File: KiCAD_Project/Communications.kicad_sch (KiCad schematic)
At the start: 19 parts, among them J14 1-0000050, J15 1-0000190, U10 1-0000785, U11 1-0000446

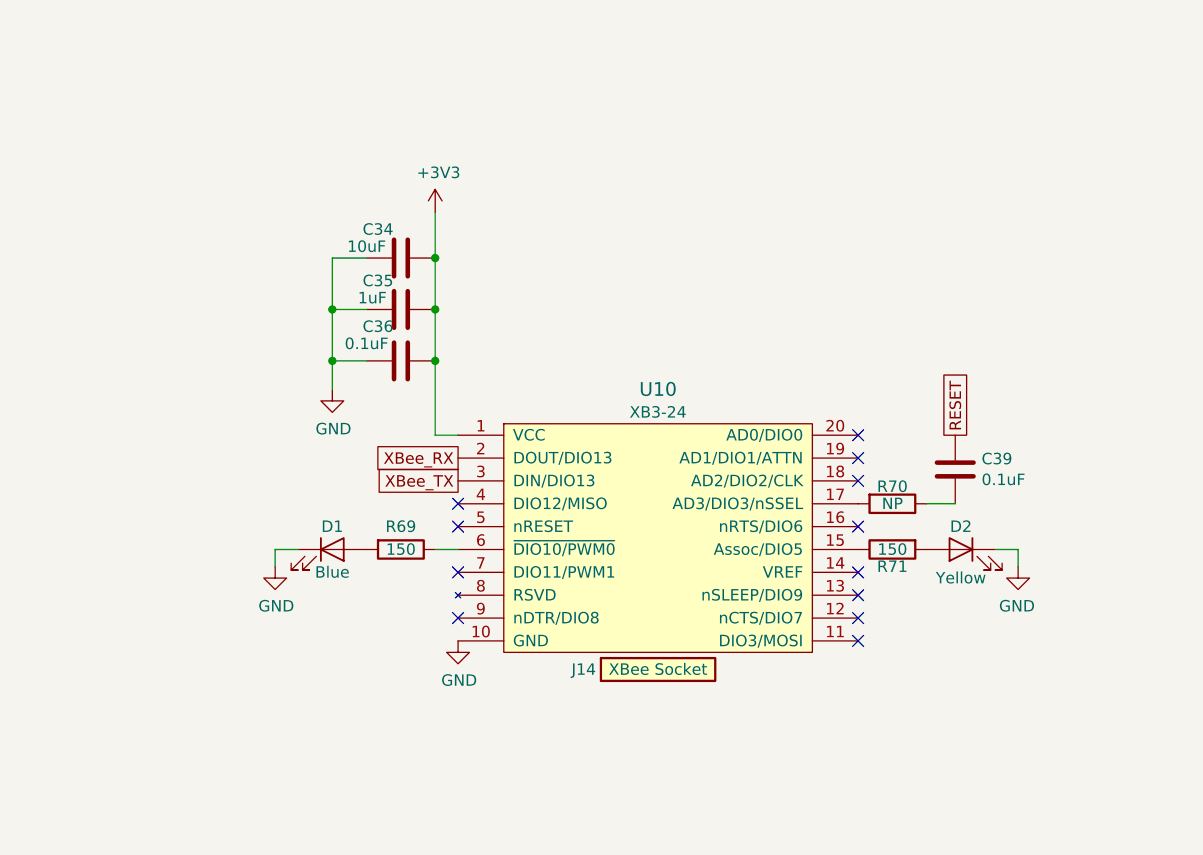
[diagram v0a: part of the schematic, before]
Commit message: Issue #2 (NP on all XBEE parts, J3 changed to SMPL)
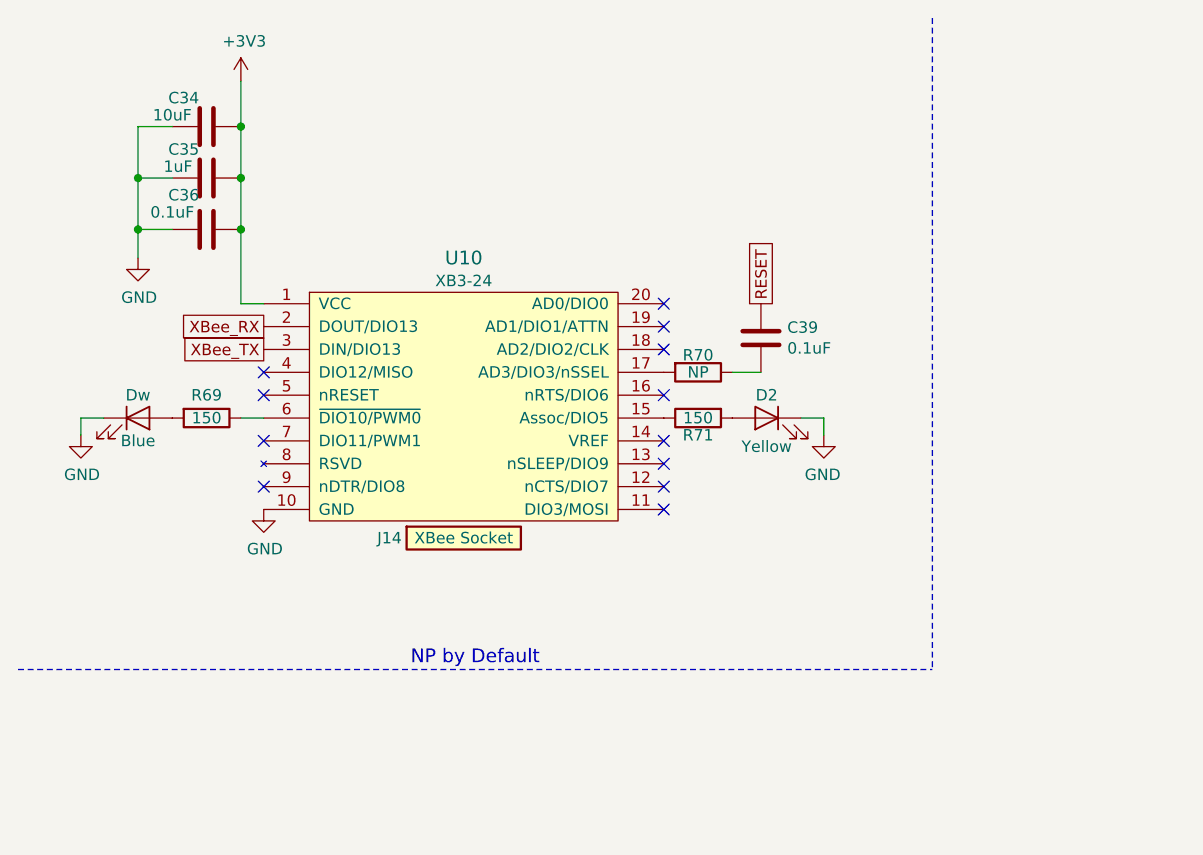
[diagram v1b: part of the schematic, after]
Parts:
- C34, C35, C36, J14, R69: Populated 1 -> 0
- Dw: renamed from D1; Populated 1 -> 0
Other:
- note added: "NP by Default"
- moved on the sheet: C34, C35, C36, C39, D2, Dw, J14, R69, R70, R71, U10

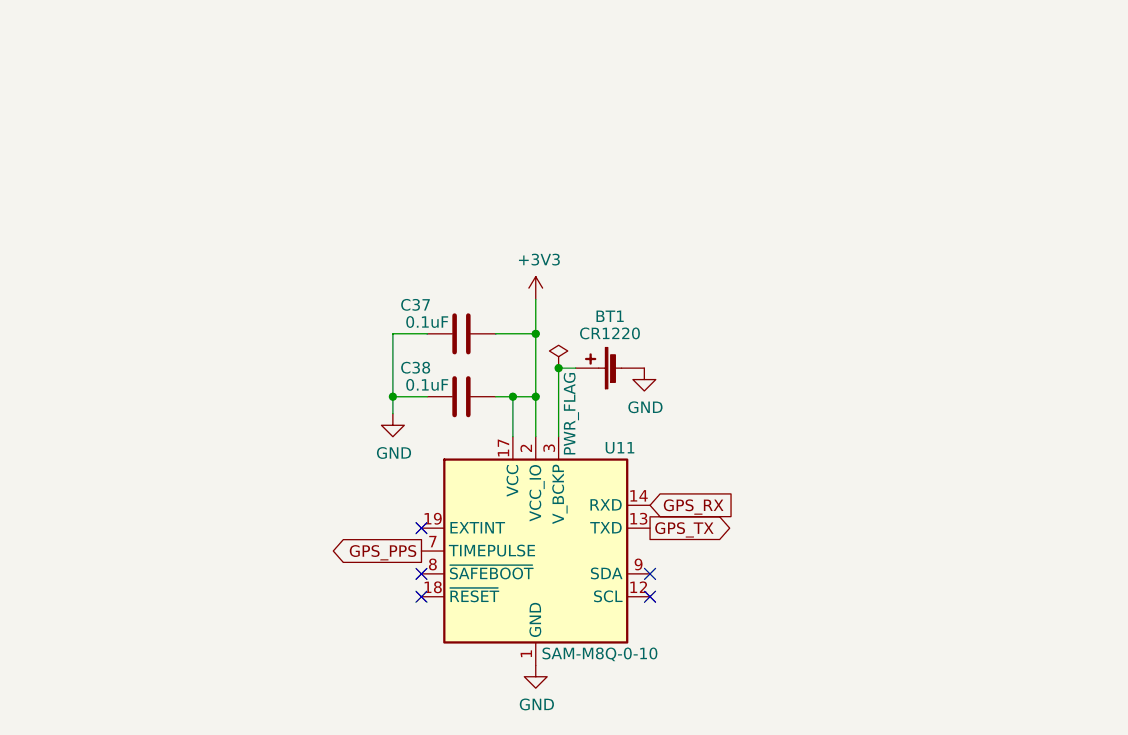
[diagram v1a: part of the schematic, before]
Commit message: Fixed Issue #5 (Replaced GPS w/ 1-464)
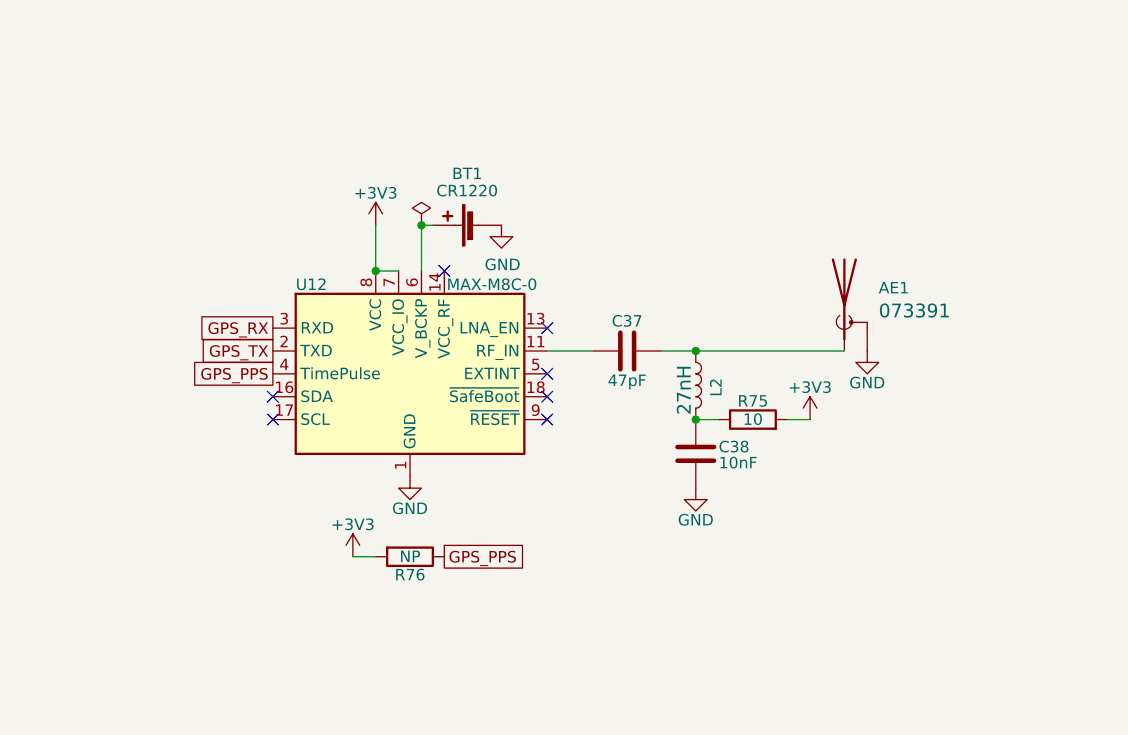
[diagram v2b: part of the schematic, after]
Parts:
- removed C37, C38: 1-0000007, capacitors_0603:1-0000007, symbol capacitors_0603:1-0000007
- removed U11: 1-0000446, others:1-0000446, symbol others:1-0000446
- added AE1: 1-0000461, connectors:1-0000461, symbol connectors:1-0000461
- added C37: 1-0000458, capacitors_0603:1-0000458, symbol capacitors_0603:1-0000458
- added C38: 1-0000014, capacitors_0603:1-0000014, symbol capacitors_0603:1-0000014
- added L2: 1-0000459, inductors_0603:1-0000459, symbol inductors_0603:1-0000459
- added R75: 1-0000678, resistors_0603:1-0000678, symbol resistors_0603:1-0000678
- added R76: 1-0000010, resistors_0603:1-0000010, symbol resistors_0603:1-0000010
- added U12: 1-0000464, others:1-0000464, symbol others:1-0000464
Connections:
- net +3V3: now also R75.2, R76.2, U12.7 (VCC_IO), U12.8 (VCC)
- net GND: now also AE1.2 (Shield), C38.2, U12.1 (GND), U12.10 (GND), U12.12 (GND)
- net GPS_PPS: now also R76.1, U12.4 (TimePulse)
- net GPS_RX: now also U12.3 (RXD)
- net GPS_TX: now also U12.2 (TXD)
- net at BT1.1 (+): now also U12.6 (V_BCKP)
- new net: C37.1, U12.11 (RF_IN)
- new net: AE1.1 (A), C37.2, L2.1
- new net: C38.1, L2.2, R75.1
- no-connect marks 17 -> 19
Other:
- moved on the sheet: BT1

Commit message: Schematic ERC Issue Cleanup
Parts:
- removed Dw: 1-0000599, leds_0805:1-0000599, symbol leds_0805:1-0000599
- added D4: 1-0000599, leds_0805:1-0000599, symbol leds_0805:1-0000599
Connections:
- net GND: now also D4.1 (K)
- net at R69.2: now also D4.2 (A)
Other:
- moved on the sheet: C34, C35, C36, C40, D2, J14, J15, R69, R70, R71, R72, R73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

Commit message: Revised Layout for Rev2.0 Changes
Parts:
- renumbered C34 to C23, C35 to C24, C36 to C25, C37 to C26, C39 to C27, C38 to C28, C40 to C29, D4 to D3, D2 to D4, J14 to J11, J15 to J12, R69 to R33, R76 to R34, R70 to R35, R71 to R36, R75 to R37, R72 to R38, R73 to R39, U12 to U11

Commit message: Fixed Populated fleild setting on XBEE Componenets
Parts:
- D3, D4, R36, U10: Populated 1 -> 0
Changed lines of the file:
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@@
 			"AAAAAAAAAAAAAAAAAAAAAAAAAAAAAAAAAAAAAAAAAAAAAAAAAAAAAAAAAAAAAAAAAAAAAAAAAAAA"
 			"AAAAAAAAAAAAAAAAAAAAAAAAAAAAAAAAAAAAAAAAAAAAAAAAAAAAAAAAAAAAAAAAAAAAAAAAAAAA"
-			"AAAAAAAAAA=="
+			"AAAAAAAAAAAAAACljUAuAEwCgAAAAAAAAAAAAwAAAAAAAABAj9h7vwEAAAEAAAAAAAAAAAAAAAAA"
+			"AAC4jV0uAE0CgEBX+nu/AQAAAwAAAAAAAACAith7vwEAAAEAAAAAAAAAAAAAAAAAAAC/jV4uAE4C"
+			"gIBW+nu/AQAAAwAAAAAAAAAA1Pl7vwEAAAEAAAAAAAAAAAAAAAAAAACyjVsuAE8CgEM6L1dJTkRP"
+			"V1MvZm9udHNcQ0hJTExFUi5UVEYAAAAAAAAAAAAAAACxjVQuAFACgMBS+nu/AQAAAwAAAAAAAAAg"
+			"idh7vwEAAAEAAAAAAAAAAAAAAAAAAAC0jVEuAFECgBBR+nu/AQAAAwAAAAAAAABg0/l7vwEAAAEA"
+			"AAAAAAAAAAAAAAAAAABLjFIuAFICgEM6L1dJTkRPV1MvZm9udHNcQ09MT05OQS5UVEYAAAAAAAAA"
+			"AAAAAABOjK8vAFMCgAAAAAAAAAAAAwAAAAAAAABQ1Pl7vwEAAAEAAAAAAAAAAAAAAAAAAABNjKgv"
+			"AFQCgMBP+nu/AQAAAwAAAAAAAACg0vl7vwEAAAEAAAAAAAAAAAAAAAAAAABAjKUvAFUCgLBT+nu/"
+			"AQAAAwAAAAAAAABgjth7vwEAAAEAAAAAAAAAAAAAAAAAAABHjKYvAFYCgNBR+nu/AQAAAwAAAAAA"
+			"AABA0fl7vwEAAAEAAAAAAAAAAAAAAAAAAABajKMvAFcCgGBY+nu/AQAAAwAAAAAAAABw0vl7vwEA"
+			"AAEAAAAAAAAAAAAAAAAAAABZjLwvAFgCgFBT+nu/AQAAAwAAAAAAAACA0vl7vwEAAAEAAAAAAAAA"
+			"AAAAAAAAAABcjLkvAFkCgJBY+nu/AQAAAwAAAAAAAAAA0vl7vwEAAAEAAAAAAAAAAAAAAAAAAABT"
+			"jLovAFoCgAAAAAAAAAAAAwAAAAAAAAAgjNh7vwEAAAEAAAAAAAAAAAAAAAAAAABWjLcvAFsCgMBM"
+			"+nu/AQAAAwAAAAAAAACgjNh7vwEAAAEAAAAAAAAAAAAAAAAAAABVjLAvAFwCgAAAAAAAAAAABAAA"
+			"AAAAAAABAAAAAAAAAAEAAAAAAAAAAAAAAAAAAABojI0vAF0CgAAAAAAAAAAAAwAAAAAAAABw0/l7"
+			"vwEAAAEAAAAAAAAAAAAAAAAAAABvjI4vAF4CgJBS+nu/AQAAAwAAAAAAAABgi9h7vwEAAAEAAAAA"
+			"AAAAAAAAAAAAAABijIsvAF8CgCBT+nu/AQAAAwAAAAAAAADgidh7vwEAAAEAAAAAAAAAAAAAAAAA"
+			"AABhjIQvAGACgGBV+nu/AQAAAwAAAAAAAADAidh7vwEAAAEAAAAAAAAAAAAAAAAAAABkjIEvAGEC"
+			"gFBQ+nu/AQ=="
 		)
 	)
@@
 			)
 		)
-		(property "Populated" "1"
+		(property "Populated" "0"
 			(at 96.52 58.42 0)
 			(effects
@@
 			)
 		)
-		(property "Populated" "1"
+		(property "Populated" "0"
 			(at 62.865 57.15 0)
 			(effects
@@
 			)
 		)
-		(property "Populated" "1"
+		(property "Populated" "0"
 			(at 88.9 58.42 0)
 			(effects
@@
 			)
 		)
-		(property "Populated" "1"
+		(property "Populated" "0"
 			(at 28.575 58.42 0)
 			(effects
